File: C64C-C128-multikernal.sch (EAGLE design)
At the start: 15 parts, among them IC1 27C256/512, IC2 MICROCHIP_PIC12F629P

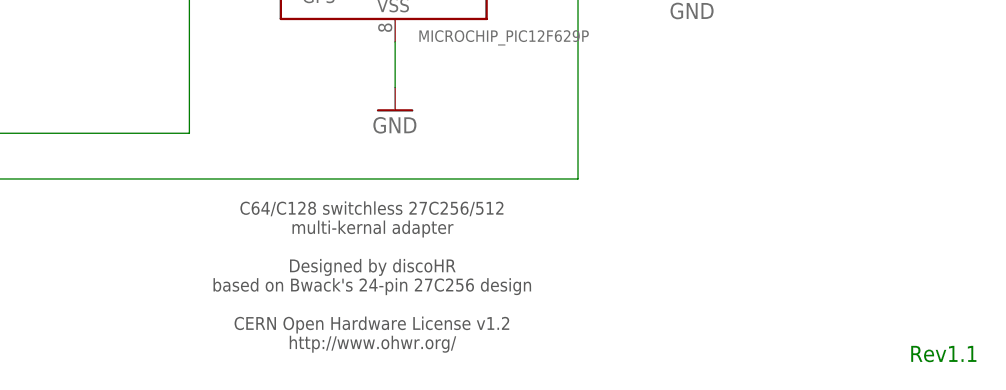
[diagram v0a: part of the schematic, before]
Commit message: expanded the pcb a bit increased the distance between EPROM and connectors increased font sizes moved some texts to the bottom added CERN OHL and GitHub URL to the silkscreen finalized rev1.1
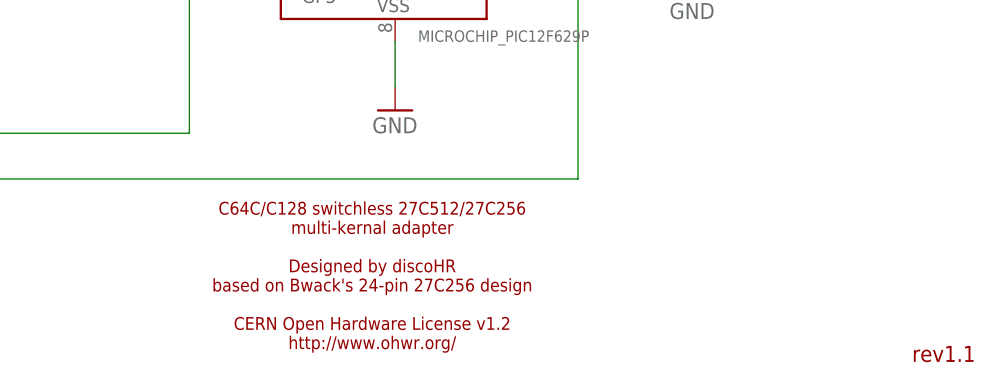
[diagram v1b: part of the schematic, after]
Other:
- note added: "C64C/C128 switchless 27C512/27C256 multi-kernal adapter Designed by discoHR based on Bwack's 24-pin 27C256 design CERN Open Hardware License v1.2 http://www.ohwr.org/"
- note added: "rev1.1"
- note removed: "C64/C128 switchless 27C256/512 multi-kernal adapter Designed by discoHR based on Bwack's 24-pin 27C256 design CERN Open Hardware License v1.2 http://www.ohwr.org/"
- note removed: "Rev1.1"
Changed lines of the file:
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@@
 <sheet>
 <plain>
-<text x="111.76" y="22.86" size="1.4224" layer="97" align="top-center">C64/C128 switchless 27C256/512
+<text x="111.76" y="22.86" size="1.4224" layer="94" font="vector" align="top-center">C64C/C128 switchless 27C512/27C256
 multi-kernal adapter
 Designed by discoHR
@@
 CERN Open Hardware License v1.2
 http://www.ohwr.org/</text>
-<text x="175.26" y="5.08" size="1.778" layer="91" align="bottom-center">Rev1.1</text>
+<text x="175.26" y="5.08" size="1.778" layer="94" font="vector" align="bottom-center">rev1.1</text>
 </plain>
 <instances>
@@
 <instance part="IC2" gate="G$1" x="111.76" y="50.8" smashed="yes">
 <attribute name="NAME" x="101.6" y="62.23" size="1.778" layer="95"/>
-<attribute name="VALUE" x="116.84" y="40.64" size="1.27" layer="96"/>
+<attribute name="VALUE" x="116.84" y="40.64" size="1.27" layer="96" font="vector"/>
 </instance>
 <instance part="R2" gate="G$1" x="73.66" y="55.88" smashed="yes">
@@
 <instance part="GND4" gate="1" x="76.2" y="73.66"/>
 <instance part="GND5" gate="1" x="114.3" y="33.02"/>
-<instance part="FRAME1" gate="G$1" x="0" y="0"/>
+<instance part="FRAME1" gate="G$1" x="0" y="0" smashed="yes">
+<attribute name="DRAWING_NAME" x="140.97" y="15.24" size="2.1844" layer="94" font="vector"/>
+<attribute name="LAST_DATE_TIME" x="140.97" y="10.16" size="2.1844" layer="94" font="vector"/>
+<attribute name="SHEET" x="154.305" y="5.08" size="2.1844" layer="94" font="vector"/>
+</instance>
 <instance part="SJ1" gate="1" x="139.7" y="53.34" rot="R180"/>
 <instance part="GND2" gate="1" x="55.88" y="40.64"/>
